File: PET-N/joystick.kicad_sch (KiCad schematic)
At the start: 1 part

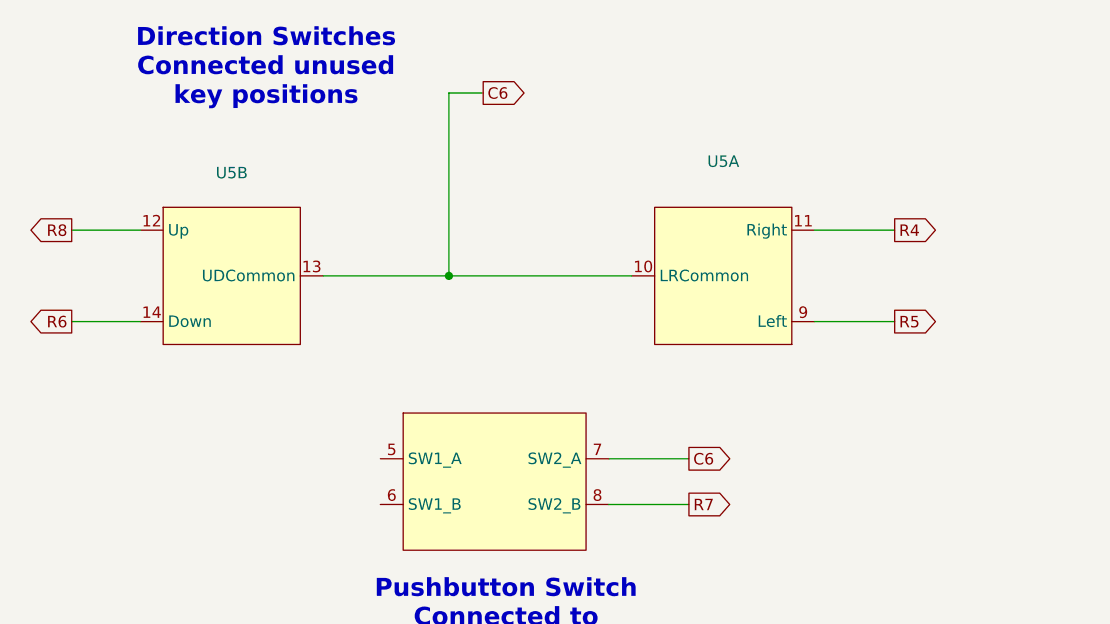
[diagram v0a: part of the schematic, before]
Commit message: fix Cn vs CCn bug, add proper joystick in schem; routing still to fix
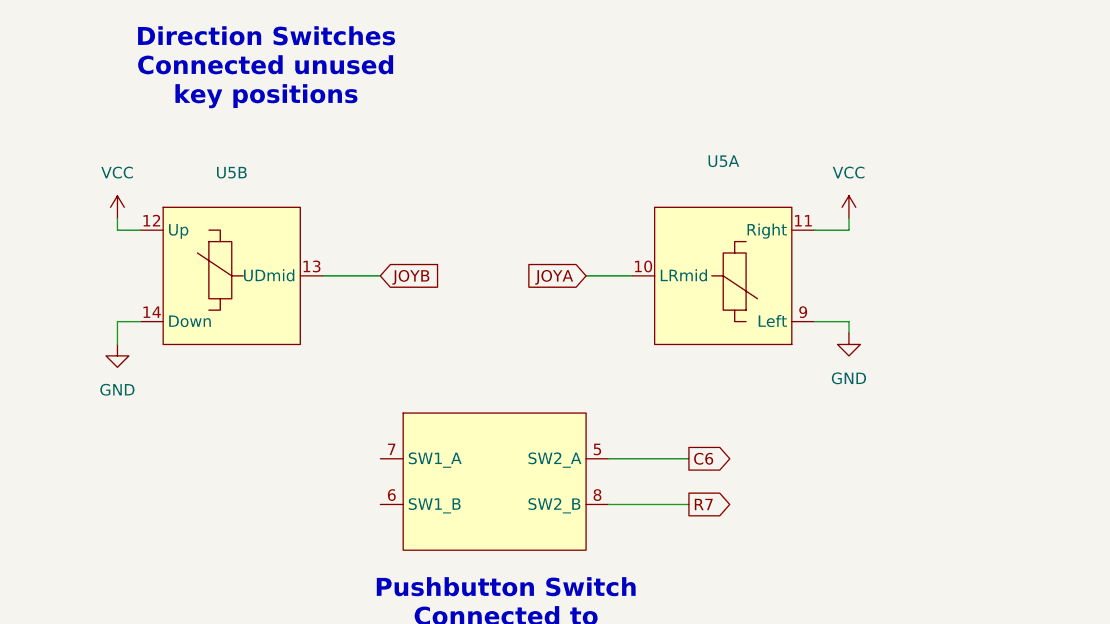
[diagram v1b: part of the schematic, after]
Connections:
- net R6 is gone; now on net GND: U5.14 (Down)
- net R8 is gone; now on net VCC: U5.12 (Up)
- net C6: now also U5.5 (SW2_A); no longer U5.10 (LRCommon), U5.13 (UDCommon), U5.7 (SW2_A)
- net R4 renamed VCC
- net R5 renamed GND
- new net JOYA: U5.10 (LRmid)
- new net JOYB: U5.13 (UDmid)

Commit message: hopefully final schem and layout for 3.0A
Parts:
- added JC1, JC2, JC3, JC4, JC5, JC6, JC7, JC8: SolderJumper_2_Bridged, Jumper:SolderJumper-2_P1.3mm_Open_RoundedPad1.0x1.5mm, symbol Jumper:SolderJumper_2_Open
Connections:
- net C6: now also JC6.2 (B)
- new net C1: JC1.2 (B)
- new net C2: JC2.2 (B)
- new net C3: JC3.2 (B)
- new net C4: JC4.2 (B)
- new net C5: JC5.2 (B)
- new net C7: JC7.2 (B)
- new net C8: JC8.2 (B)
- new net CC1: JC1.1 (A)
- new net CC2: JC2.1 (A)
- new net CC3: JC3.1 (A)
- new net CC4: JC4.1 (A)
- new net CC5: JC5.1 (A)
- new net CC6: JC6.1 (A)
- new net CC7: JC7.1 (A)
- new net CC8: JC8.1 (A)
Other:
- note added: "CBM-KEYB-PETN-3.0A-20251011"
- note added: "Solder all JC1..JC8 if you use the original connector, or leave out the keyboard controller"
- note removed: "CBM-KEYB-PETN-3.0-20251005"

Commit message: as sent to production
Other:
- note added: "CBM-KEYB-PETN-3.0A-20251014"
- note removed: "CBM-KEYB-PETN-3.0A-20251011"
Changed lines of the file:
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@@
 	(generator_version "9.0")
 	(paper "A4")
-	(text "CBM-KEYB-PETN-3.0A-20251011"
+	(text "CBM-KEYB-PETN-3.0A-20251014"
 		(exclude_from_sim no)
 		(at 231.14 173.736 0)

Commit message: first run on r3.1
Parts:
- removed JC1, JC2, JC3, JC4, JC5, JC6, JC7, JC8: SolderJumper_2_Bridged, Jumper:SolderJumper-2_P1.3mm_Open_RoundedPad1.0x1.5mm, symbol Jumper:SolderJumper_2_Open
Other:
- note added: "(C) 2020, 2021 Steve J. Gray (C) 2025, 2026 André Fachat"
- note added: "CBM-KEYB-PETN-3.1A-20260130"
- note removed: "(C) 2020,2021 Steve J. Gray (C) 2025 André Fachat"
- note removed: "CBM-KEYB-PETN-3.0A-20251014"
- note removed: "Solder all JC1..JC8 if you use the original connector, or leave out the keyboard controller"

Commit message: add orientation marker for backlight LEDs and move to 3.1B
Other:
- note added: "CBM-KEYB-PETN-3.1B-20260405"
- note removed: "CBM-KEYB-PETN-3.1A-20260130"
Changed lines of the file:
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@@
 	(generator_version "9.0")
 	(paper "A4")
-	(text "CBM-KEYB-PETN-3.1A-20260130"
+	(text "CBM-KEYB-PETN-3.1B-20260405"
 		(exclude_from_sim no)
 		(at 229.87 174.625 0)
